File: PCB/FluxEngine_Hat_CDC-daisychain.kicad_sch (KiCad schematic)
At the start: 3 parts, among them J1 CY8CKIT-059, P1 FDC_BUS_IBMPC, P2 FDC_BUS_CDC_DaisyChain

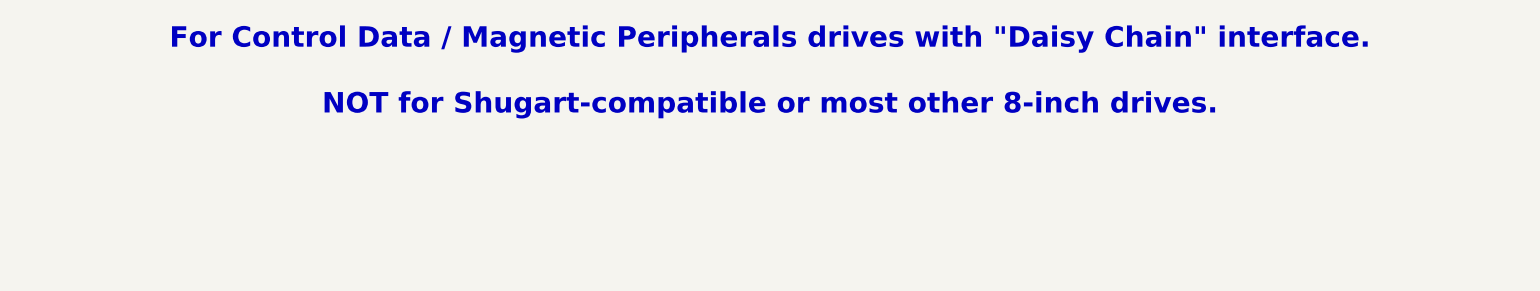
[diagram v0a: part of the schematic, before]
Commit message: Combined CDC new & old standard interface
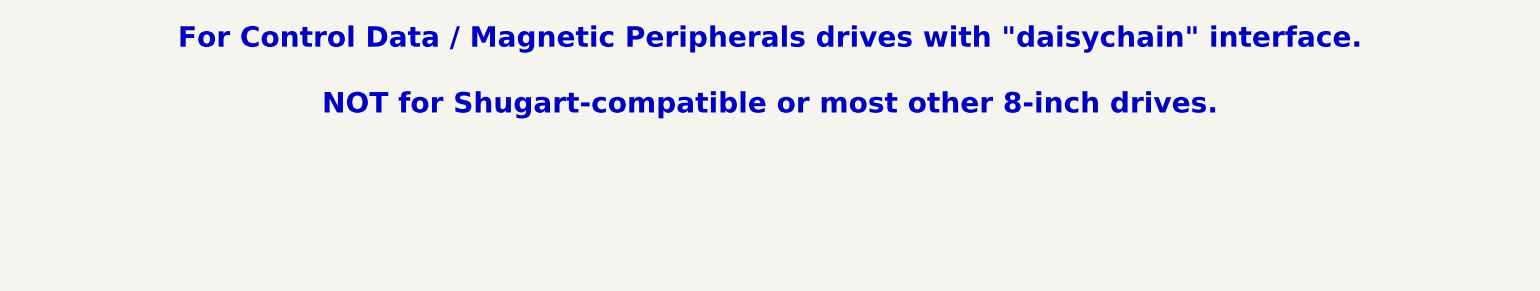
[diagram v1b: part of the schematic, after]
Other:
- note added: "For Control Data / Magnetic Peripherals drives with "daisychain" interface. NOT for Shugart-compatible or most other 8-inch drives."
- note removed: "For Control Data / Magnetic Peripherals drives with "Daisy Chain" interface. NOT for Shugart-compatible or most other 8-inch drives."
- title: FluxEngine_Hat for PC and CDC DaisyChain -> FluxEngine_Hat for PC and CDC-daisychain
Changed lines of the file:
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@@
 	(paper "User" 298.45 217.322)
 	(title_block
-		(title "FluxEngine_Hat for PC and CDC DaisyChain")
-		(date "2024-04-29")
-		(rev "002")
+		(title "FluxEngine_Hat for PC and CDC-daisychain")
+		(date "2024-04-30")
+		(rev "003")
 		(company "Brian K. White - b.kenyon.w@gmail.com")
 		(comment 1 "CC BY-SA")
@@
 		)
 	)
-	(text "For Control Data / Magnetic Peripherals drives with \"Daisy Chain\" interface.\n\nNOT for Shugart-compatible or most other 8-inch drives.\n"
+	(text "For Control Data / Magnetic Peripherals drives with \"daisychain\" interface.\n\nNOT for Shugart-compatible or most other 8-inch drives.\n"
 		(exclude_from_sim no)
 		(at 152.908 38.608 0)
@@
 		)
 		(instances
-			(project "FluxEngine_Hat_CDC_DaisyChain"
+			(project "FluxEngine_Hat_CDC-daisychain"
 				(path "/72d4cbf5-bf28-4978-b5d4-f13155888c6e"
 					(reference "#PWR06")
@@
 		)
 		(instances
-			(project "FluxEngine_Hat_CDC_DaisyChain"
+			(project "FluxEngine_Hat_CDC-daisychain"
 				(path "/72d4cbf5-bf28-4978-b5d4-f13155888c6e"
 					(reference "J1")
@@
 		)
 		(instances
-			(project "FluxEngine_Hat_CDC_DaisyChain"
+			(project "FluxEngine_Hat_CDC-daisychain"
 				(path "/72d4cbf5-bf28-4978-b5d4-f13155888c6e"
 					(reference "P2")
@@
 		)
 		(instances
-			(project "FluxEngine_Hat_CDC_DaisyChain"
+			(project "FluxEngine_Hat_CDC-daisychain"
 				(path "/72d4cbf5-bf28-4978-b5d4-f13155888c6e"
 					(reference "#PWR08")
@@
 		)
 		(instances
-			(project "FluxEngine_Hat_CDC_DaisyChain"
+			(project "FluxEngine_Hat_CDC-daisychain"
 				(path "/72d4cbf5-bf28-4978-b5d4-f13155888c6e"
 					(reference "P1")
@@
 		)
 		(instances
-			(project "FluxEngine_Hat_CDC_DaisyChain"
+			(project "FluxEngine_Hat_CDC-daisychain"
 				(path "/72d4cbf5-bf28-4978-b5d4-f13155888c6e"
 					(reference "#PWR07")
@@
 		)
 		(instances
-			(project "FluxEngine_Hat_CDC_DaisyChain"
+			(project "FluxEngine_Hat_CDC-daisychain"
 				(path "/72d4cbf5-bf28-4978-b5d4-f13155888c6e"
 					(reference "#PWR02")
@@
 		)
 		(instances
-			(project "FluxEngine_Hat_CDC_DaisyChain"
+			(project "FluxEngine_Hat_CDC-daisychain"
 				(path "/72d4cbf5-bf28-4978-b5d4-f13155888c6e"
 					(reference "#PWR04")

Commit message: staggered rows offset & direction
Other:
- title: FluxEngine_Hat for PC and CDC-daisychain -> FluxEngine_Hat_CDC-daisychain
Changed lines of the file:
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@@
 	(paper "User" 298.45 217.322)
 	(title_block
-		(title "FluxEngine_Hat for PC and CDC-daisychain")
-		(date "2024-04-30")
+		(title "FluxEngine_Hat_CDC-daisychain")
+		(date "2024-08-08")
 		(rev "003")
 		(company "Brian K. White - b.kenyon.w@gmail.com")
